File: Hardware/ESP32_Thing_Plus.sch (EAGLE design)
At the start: 40 parts, among them J1 AMP FCI 10103594-0001LF, Q1 2.5A/30V, Q2 MBT3904DW1T1, U1 MCP73831, U2 ESP-WROOM-32NARROW, U3 AP2112K-3.3V, U4 CP2102N

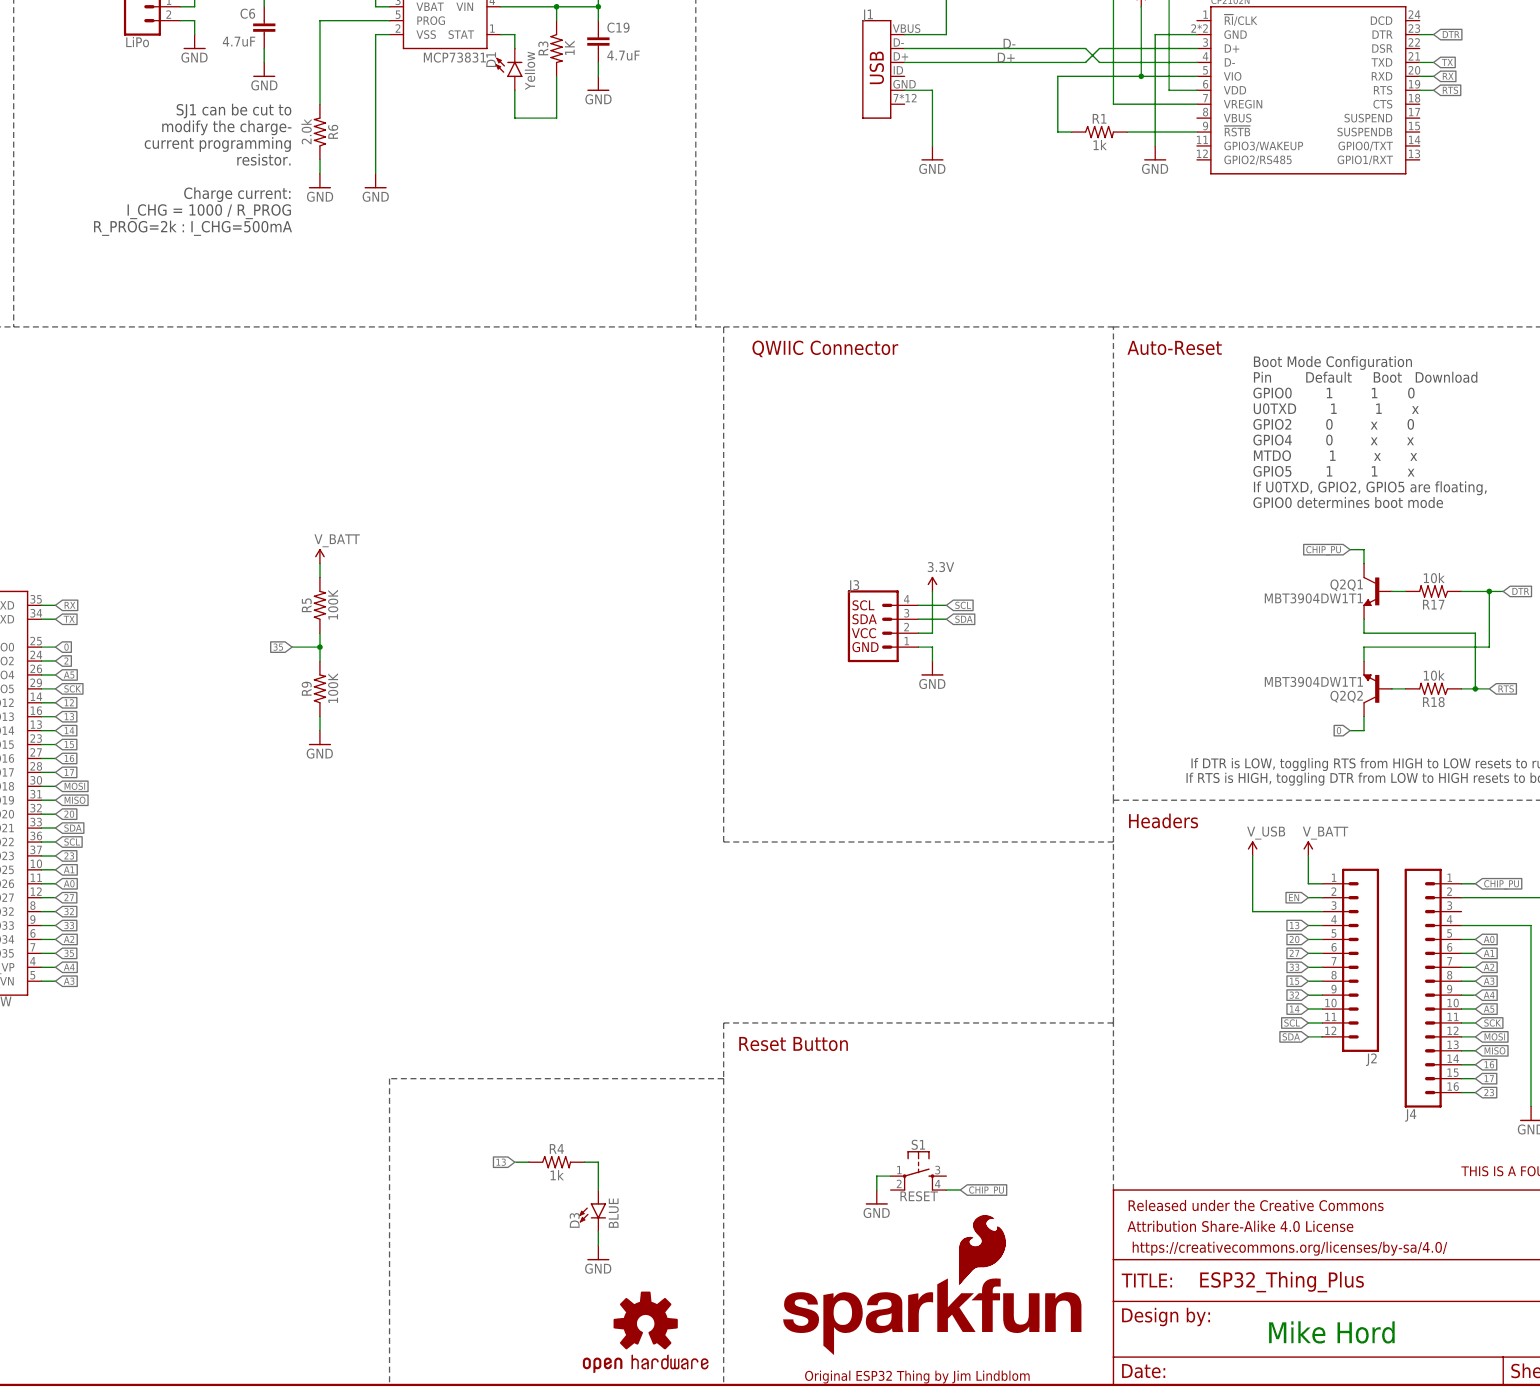
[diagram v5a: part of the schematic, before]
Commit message: Fixes after QC review
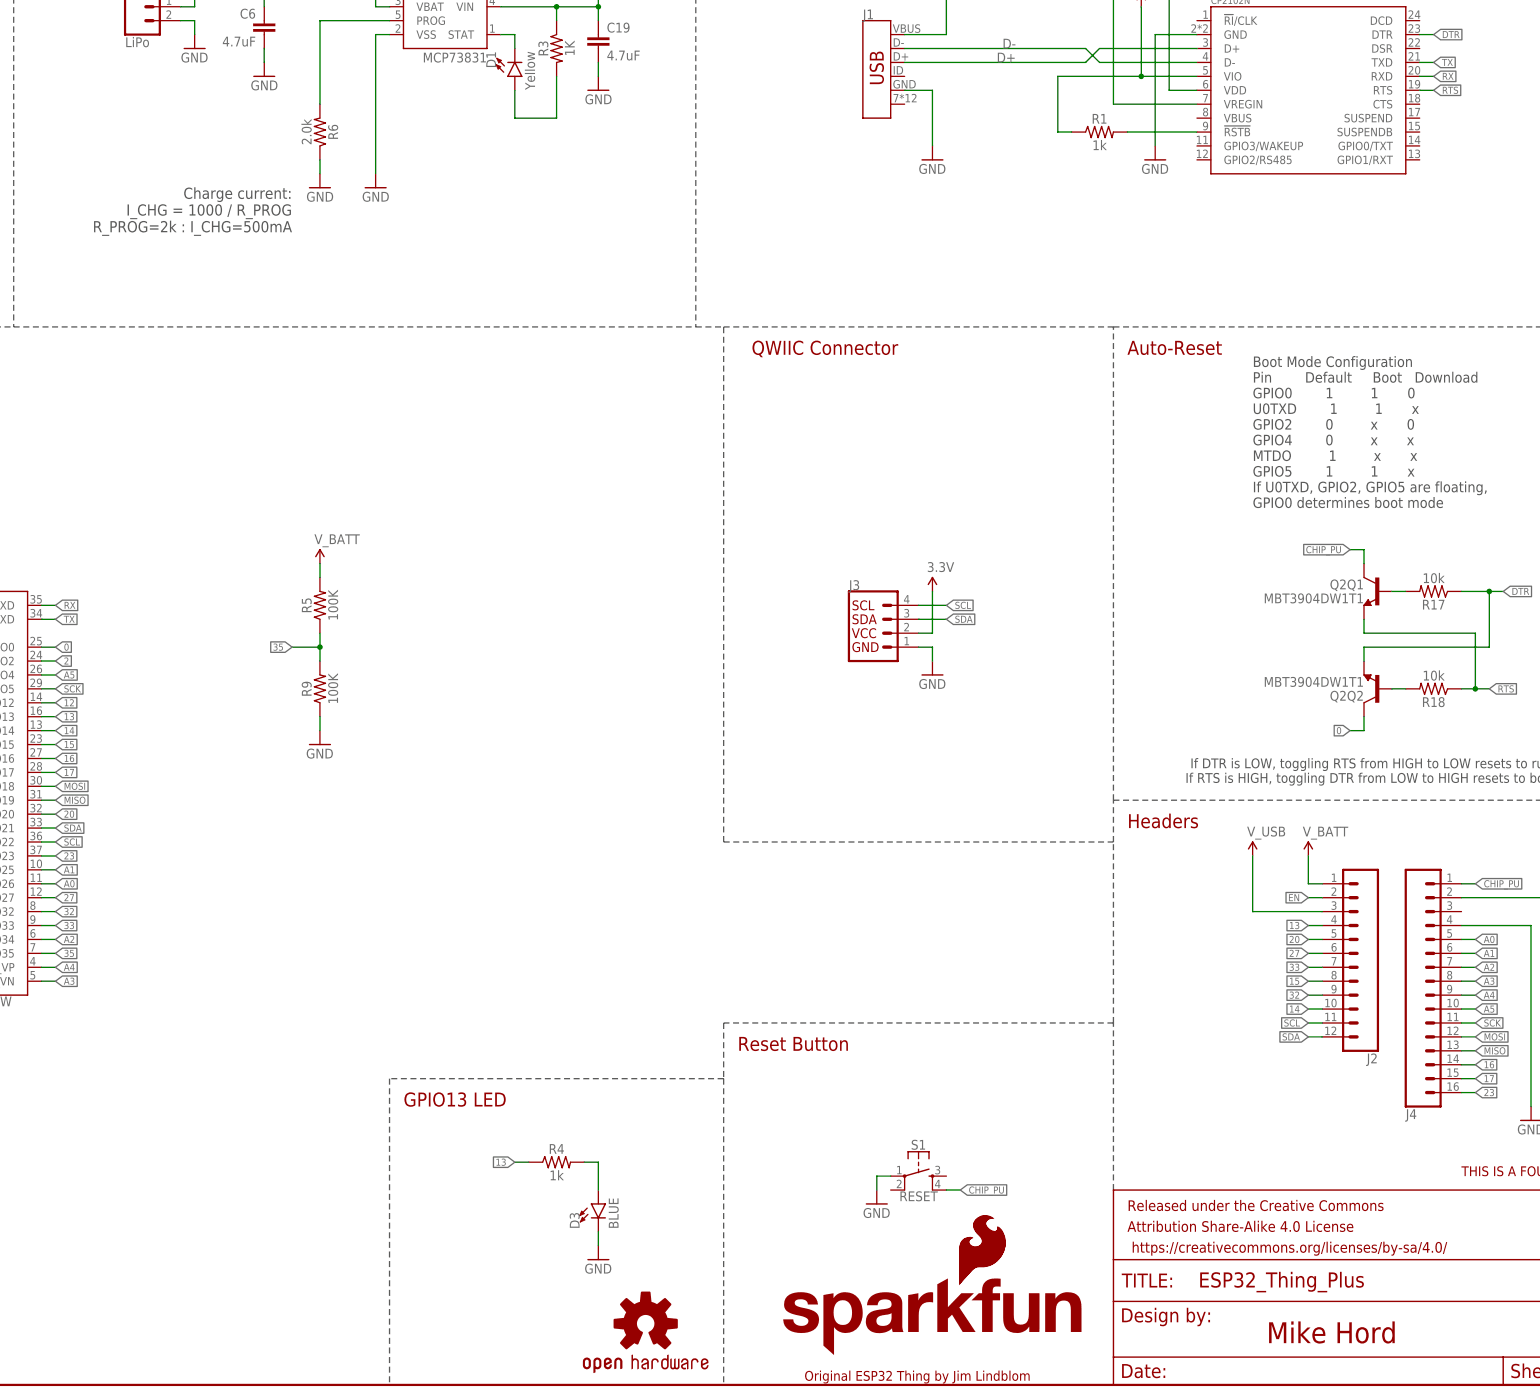
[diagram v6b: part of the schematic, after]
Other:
- note added: "GPIO13 LED"
- note removed: "SJ1 can be cut to modify the charge- current programming resistor."
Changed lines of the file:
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@@
 R_PROG=2k : I_CHG=500mA</text>
 <text x="2.54" y="276.86" size="2.54" layer="94" font="vector" align="top-left">Voltage Regulator and Battery Charger</text>
-<text x="180.34" y="233.68" size="2.032" layer="97" rot="MR0" align="top-left">SJ1 can be cut to
-modify the charge-
-current programming
-resistor.</text>
 <text x="132.08" y="276.86" size="2.54" layer="94" font="vector" align="top-left">Lithium-Polymer Battery Charger (1-cell)</text>
 <text x="86.36" y="220.98" size="1.778" layer="97" font="vector" align="top-center">600mA out
@@
 <text x="264.16" y="187.96" size="2.54" layer="94" font="vector">QWIIC Connector</text>
 <wire x1="259.08" y1="99.06" x2="259.08" y2="193.04" width="0.1524" layer="97" style="longdash"/>
-<text x="358.14" y="7.62" size="3.81" layer="91">Mike Hord</text>
+<text x="358.14" y="7.62" size="3.81" layer="94">Mike Hord</text>
+<text x="200.66" y="50.8" size="2.54" layer="94" font="vector">GPIO13 LED</text>
 </plain>
 <instances>

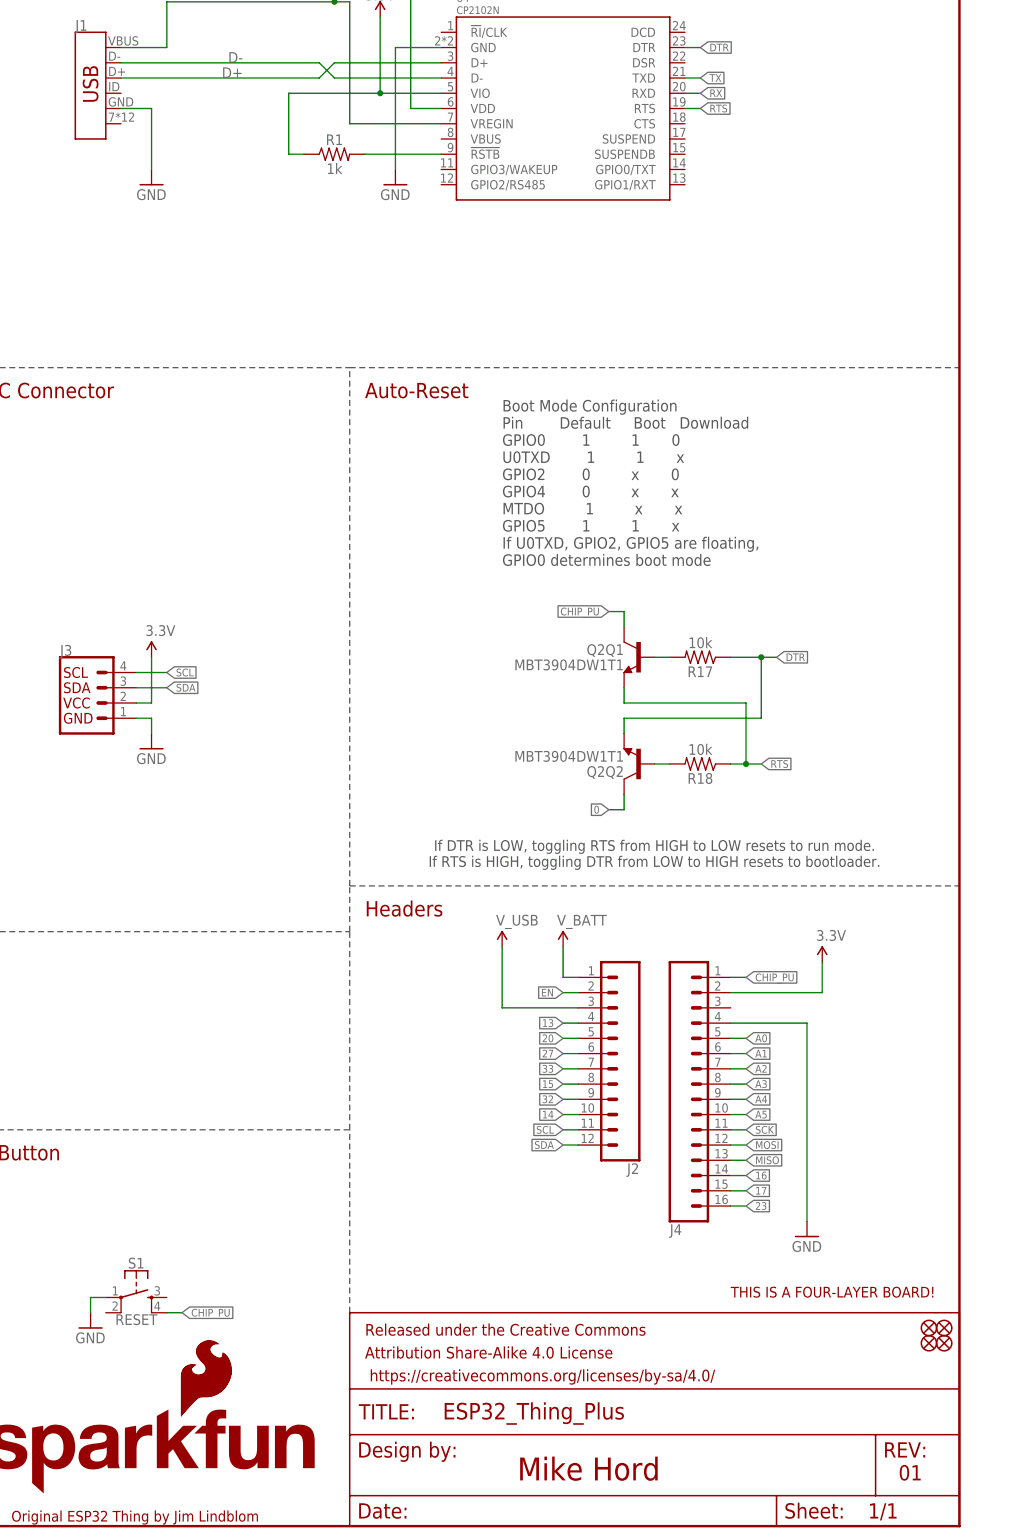
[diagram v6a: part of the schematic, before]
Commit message: Changes from review, changed silk
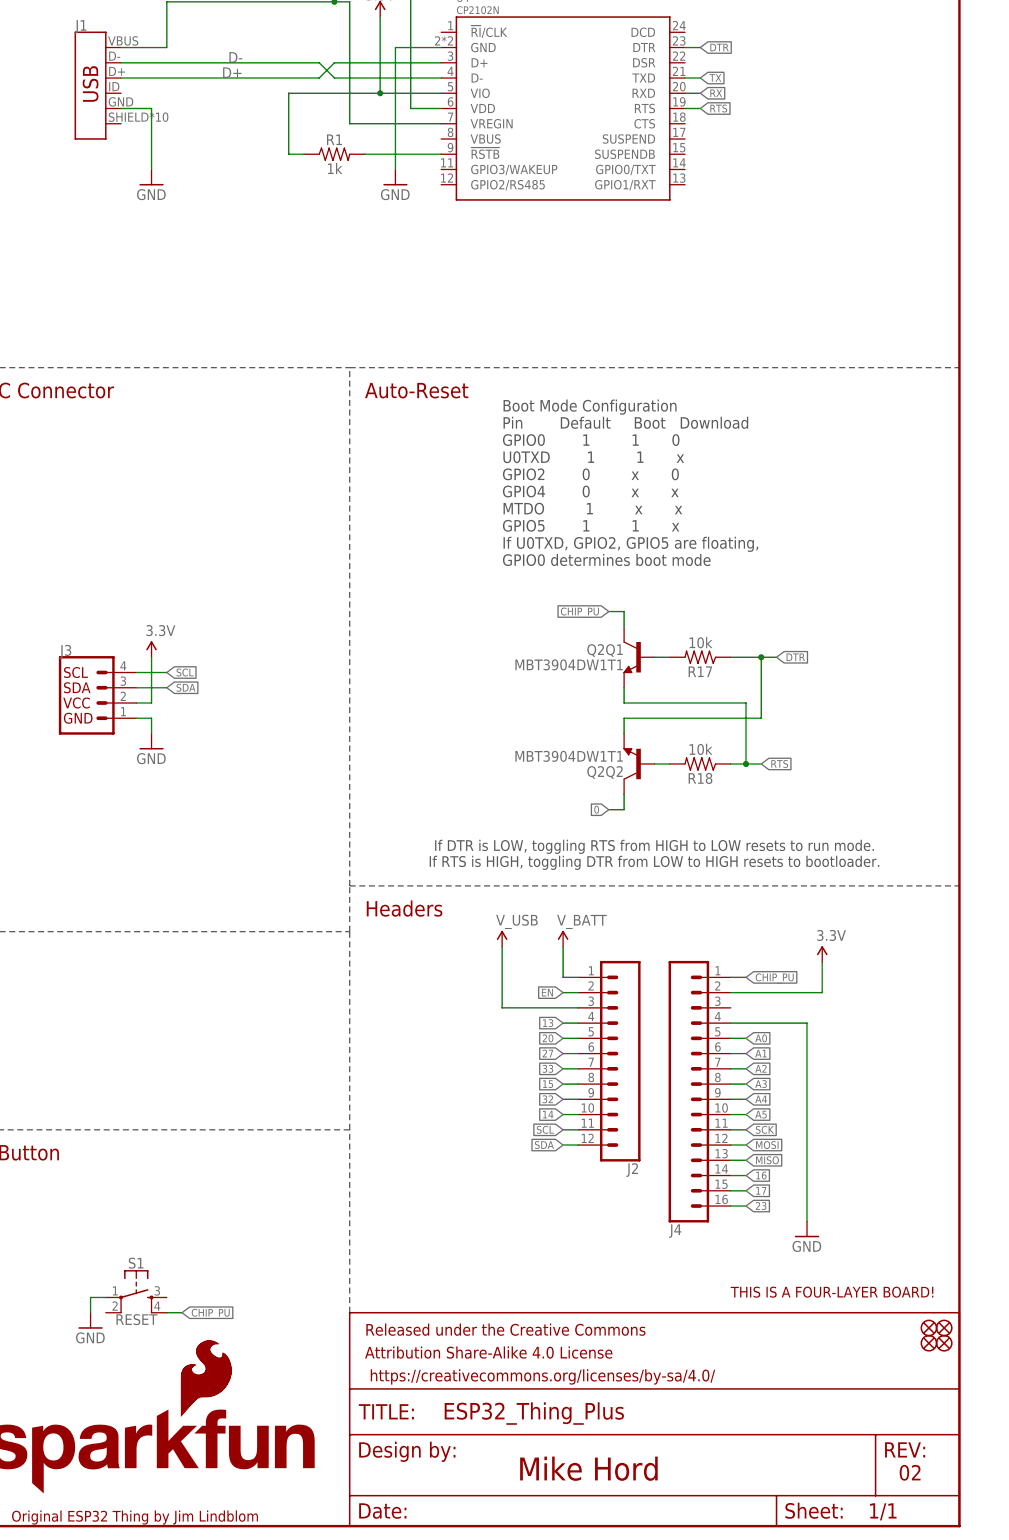
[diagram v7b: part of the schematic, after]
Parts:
- J1: device SparkFun-Connectors:USB_MICRO-B_HALF_PTH -> SparkFun-Connectors:USB_MICRO-B_HALF_PTH_MILL
- J2: device SparkFun-Connectors:CONN_12NO_SILK -> SparkFun-Connectors:CONN_12SM_SQ_NO_SILK
- J4: device SparkFun-Connectors:CONN_161X16_NO_SILK -> SparkFun-Connectors:CONN_161X16_SM_SQ_NOSILK
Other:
- note added: "02"
- note removed: "01"
- moved on the sheet: J1
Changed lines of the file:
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@@
 <part name="SUPPLY1" library="SparkFun-Aesthetics" deviceset="3.3V" device=""/>
 <part name="GND6" library="SparkFun-Aesthetics" deviceset="GND" device=""/>
-<part name="J1" library="SparkFun-Connectors" deviceset="USB_MICRO-B" device="_HALF_PTH" value="AMP FCI 10103594-0001LF"/>
+<part name="J1" library="SparkFun-Connectors" deviceset="USB_MICRO-B" device="_HALF_PTH_MILL" value="AMP FCI 10103594-0001LF"/>
 <part name="U4" library="SparkFun-IC-Comms" deviceset="CP2102N" device=""/>
 <part name="R1" library="SparkFun-Resistors" deviceset="1KOHM" device="-0603-1/10W-1%" value="1k"/>
@@
 <part name="SUPPLY9" library="SparkFun-PowerSymbols" deviceset="3.3V" device=""/>
 <part name="GND7" library="SparkFun-Aesthetics" deviceset="GND" device=""/>
-<part name="J2" library="SparkFun-Connectors" deviceset="CONN_12" device="NO_SILK"/>
-<part name="J4" library="SparkFun-Connectors" deviceset="CONN_16" device="1X16_NO_SILK"/>
+<part name="J2" library="SparkFun-Connectors" deviceset="CONN_12" device="SM_SQ_NO_SILK"/>
+<part name="J4" library="SparkFun-Connectors" deviceset="CONN_16" device="1X16_SM_SQ_NOSILK"/>
 <part name="U2" library="SparkFun-RF" deviceset="ESP-WROOM-32" device="NARROW"/>
 <part name="SUPPLY3" library="SparkFun-Aesthetics" deviceset="V_BATT" device=""/>
@@
 <text x="261.62" y="63.5" size="2.54" layer="94" font="vector" align="top-left">Reset Button</text>
 <text x="332.74" y="104.14" size="2.54" layer="94" font="vector" align="top-left">Headers</text>
-<text x="421.64" y="10.16" size="2.54" layer="94" align="top-left">01</text>
+<text x="421.64" y="10.16" size="2.54" layer="94" align="top-left">02</text>
 <text x="273.812" y="0.762" size="1.778" layer="94" rot="MR180" align="top-left">Original ESP32 Thing by Jim Lindblom</text>
 <text x="381" y="114.3" size="1.778" layer="97" font="vector" align="top-center">If DTR is LOW, toggling RTS from HIGH to LOW resets to run mode.

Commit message: Add prod_id to wroom module
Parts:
- U2: PROD_ID (none) -> IC-13849
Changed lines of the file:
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@@
 <part name="J2" library="SparkFun-Connectors" deviceset="CONN_12" device="SM_SQ_NO_SILK"/>
 <part name="J4" library="SparkFun-Connectors" deviceset="CONN_16" device="1X16_SM_SQ_NOSILK"/>
-<part name="U2" library="SparkFun-RF" deviceset="ESP-WROOM-32" device="NARROW"/>
+<part name="U2" library="SparkFun-RF" deviceset="ESP-WROOM-32" device="NARROW">
+<attribute name="PROD_ID" value="IC-13849"/>
+</part>
 <part name="SUPPLY3" library="SparkFun-Aesthetics" deviceset="V_BATT" device=""/>
 <part name="SUPPLY4" library="SparkFun-Aesthetics" deviceset="V_USB" device=""/>
@@
 <instance part="J2" gate="G$1" x="378.46" y="76.2" rot="R180"/>
 <instance part="J4" gate="G$1" x="383.54" y="71.12" rot="MR180"/>
-<instance part="U2" gate="G$1" x="116.84" y="109.22"/>
+<instance part="U2" gate="G$1" x="116.84" y="109.22">
+<attribute name="PROD_ID" x="116.84" y="109.22" size="1.27" layer="96" display="off"/>
+</instance>
 <instance part="SUPPLY3" gate="G$1" x="365.76" y="96.52" smashed="yes">
 <attribute name="VALUE" x="364.744" y="100.076" size="1.778" layer="96"/>
